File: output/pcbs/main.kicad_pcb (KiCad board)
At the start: 2 copper layers, 142.7 x 177.6 mm, 62 parts

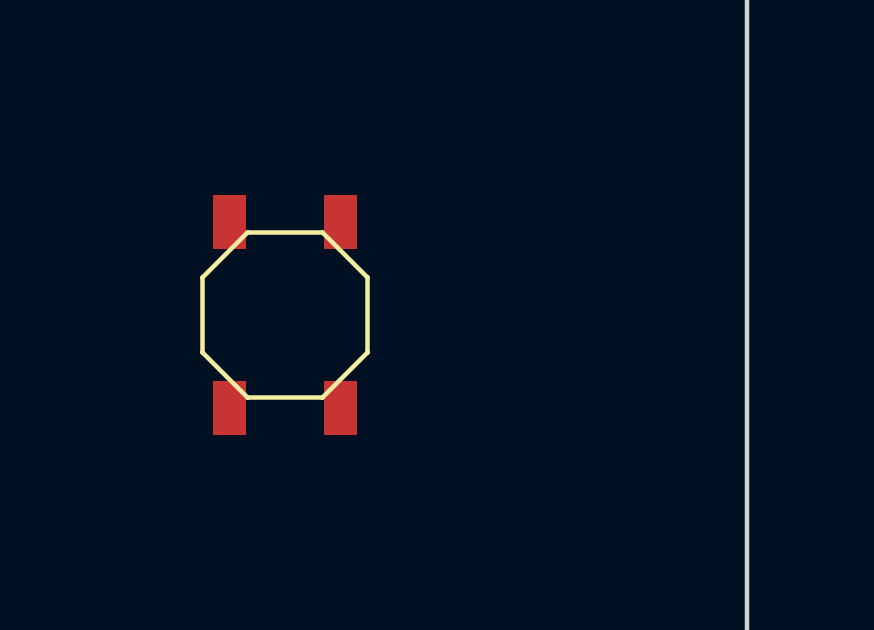
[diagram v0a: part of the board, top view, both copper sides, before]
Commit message: Fix reset position, nets
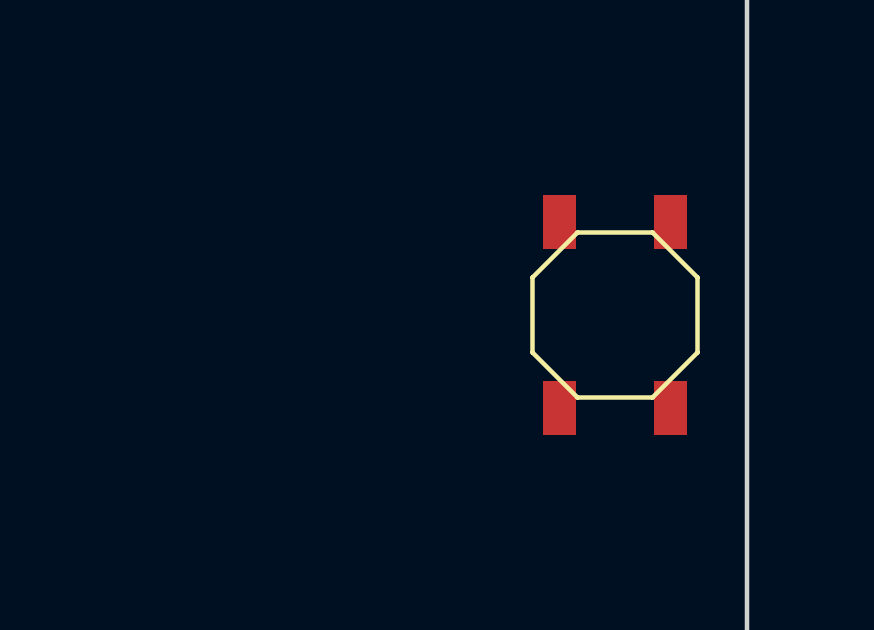
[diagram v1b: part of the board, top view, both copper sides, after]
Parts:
- moved B1 11.0 mm to (225.2, 80.5), turned to -90 degrees
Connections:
- D11 pad 1: P09 -> P9
- D12 pad 1: P08 -> P8
- D15 pad 1: P09 -> P9
- D16 pad 1: P08 -> P8
- D19 pad 1: P09 -> P9
- D20 pad 1: P08 -> P8
- D23 pad 1: P09 -> P9
- D24 pad 1: P08 -> P8
- D3 pad 1: P09 -> P9
- D4 pad 1: P08 -> P8
- D7 pad 1: P09 -> P9
- D8 pad 1: P08 -> P8
- S1 pad 1: P02 -> P2
- S10 pad 1: P04 -> P4
- S11 pad 1: P04 -> P4
- S12 pad 1: P04 -> P4
- S13 pad 1: P05 -> P5
- S14 pad 1: P05 -> P5
- S15 pad 1: P05 -> P5
- S16 pad 1: P05 -> P5
- S17 pad 1: P06 -> P6
- S18 pad 1: P06 -> P6
- S19 pad 1: P06 -> P6
- S2 pad 1: P02 -> P2
- S20 pad 1: P06 -> P6
- S21 pad 1: P07 -> P7
- S22 pad 1: P07 -> P7
- S23 pad 1: P07 -> P7
- S24 pad 1: P07 -> P7
- S25 pad 1: P02 -> P2
- S26 pad 1: P03 -> P3
- S27 pad 1: P04 -> P4
- S28 pad 1: P05 -> P5
- S29 pad 1: P06 -> P6
- S3 pad 1: P02 -> P2
- S30 pad 1: P07 -> P7
- S4 pad 1: P02 -> P2
- S5 pad 1: P03 -> P3
- S6 pad 1: P03 -> P3
- S7 pad 1: P03 -> P3
- S8 pad 1: P03 -> P3
- S9 pad 1: P04 -> P4

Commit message: Nearly viable product
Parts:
- added U?: SW-SMD_3P-P1.50_L2.7-W6.6, Switch:SW-SMD_3P-P1.50_L2.7-W6.6, F.Cu at (227.0, 92.8)
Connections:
- D1 pad 1: P16 -> P5
- D10 pad 1: P10 -> P4
- D11 pad 1: P9 -> P3
- D12 pad 1: P8 -> P2
- D13 pad 1: P16 -> P5
- D14 pad 1: P10 -> P4
- D15 pad 1: P9 -> P3
- D16 pad 1: P8 -> P2
- D17 pad 1: P16 -> P5
- D18 pad 1: P10 -> P4
- D19 pad 1: P9 -> P3
- D2 pad 1: P10 -> P4
- D20 pad 1: P8 -> P2
- D21 pad 1: P16 -> P5
- D22 pad 1: P10 -> P4
- D23 pad 1: P9 -> P3
- D24 pad 1: P8 -> P2
- D3 pad 1: P9 -> P3
- D4 pad 1: P8 -> P2
- D5 pad 1: P16 -> P5
- D6 pad 1: P10 -> P4
- D7 pad 1: P9 -> P3
- D8 pad 1: P8 -> P2
- D9 pad 1: P16 -> P5
- S1 pad 1: P2 -> P6
- S10 pad 1: P4 -> P8
- S11 pad 1: P4 -> P8
- S12 pad 1: P4 -> P8
- S13 pad 1: P5 -> P9
- S14 pad 1: P5 -> P9
- S15 pad 1: P5 -> P9
- S16 pad 1: P5 -> P9
- S17 pad 1: P6 -> P10
- S18 pad 1: P6 -> P10
- S19 pad 1: P6 -> P10
- S2 pad 1: P2 -> P6
- S20 pad 1: P6 -> P10
- S21 pad 1: P7 -> P16
- S22 pad 1: P7 -> P16
- S23 pad 1: P7 -> P16
- S24 pad 1: P7 -> P16
- S25 pad 1: P2 -> P6
- S26 pad 1: P3 -> P7
- S27 pad 1: P4 -> P8
- S28 pad 1: P5 -> P9
- S29 pad 1: P6 -> P10
- S3 pad 1: P2 -> P6
- S30 pad 1: P7 -> P16
- S4 pad 1: P2 -> P6
- S5 pad 1: P3 -> P7
- S6 pad 1: P3 -> P7
- S7 pad 1: P3 -> P7
- S8 pad 1: P3 -> P7
- S9 pad 1: P4 -> P8
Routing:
- net P14: track 0.00 -> 272.6 mm
- net P6: track 0.00 -> 253.7 mm, vias 0 -> 4
- net P7: track 0.00 -> 248.7 mm, vias 0 -> 3
- net P16: track 0.00 -> 244.0 mm, vias 0 -> 2
- net P8: track 0.00 -> 236.5 mm, vias 0 -> 3
- net P10: track 0.00 -> 235.9 mm, vias 0 -> 4
- net P9: track 0.00 -> 235.0 mm, vias 0 -> 4
- net P5: track 0.00 -> 185.3 mm
- net P4: track 0.00 -> 170.1 mm
- net P3: track 0.00 -> 155.5 mm
- net P2: track 0.00 -> 143.7 mm
- net GND: track 0.00 -> 63.5 mm
- net RST: track 0.00 -> 41.1 mm
- net sixth_cluster: track 0.00 -> 15.1 mm
- net second_cluster: track 0.00 -> 15.1 mm
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- added copper zone on B.Cu, net GND
- added copper zone on F.Cu, net GND
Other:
- net class Default removed

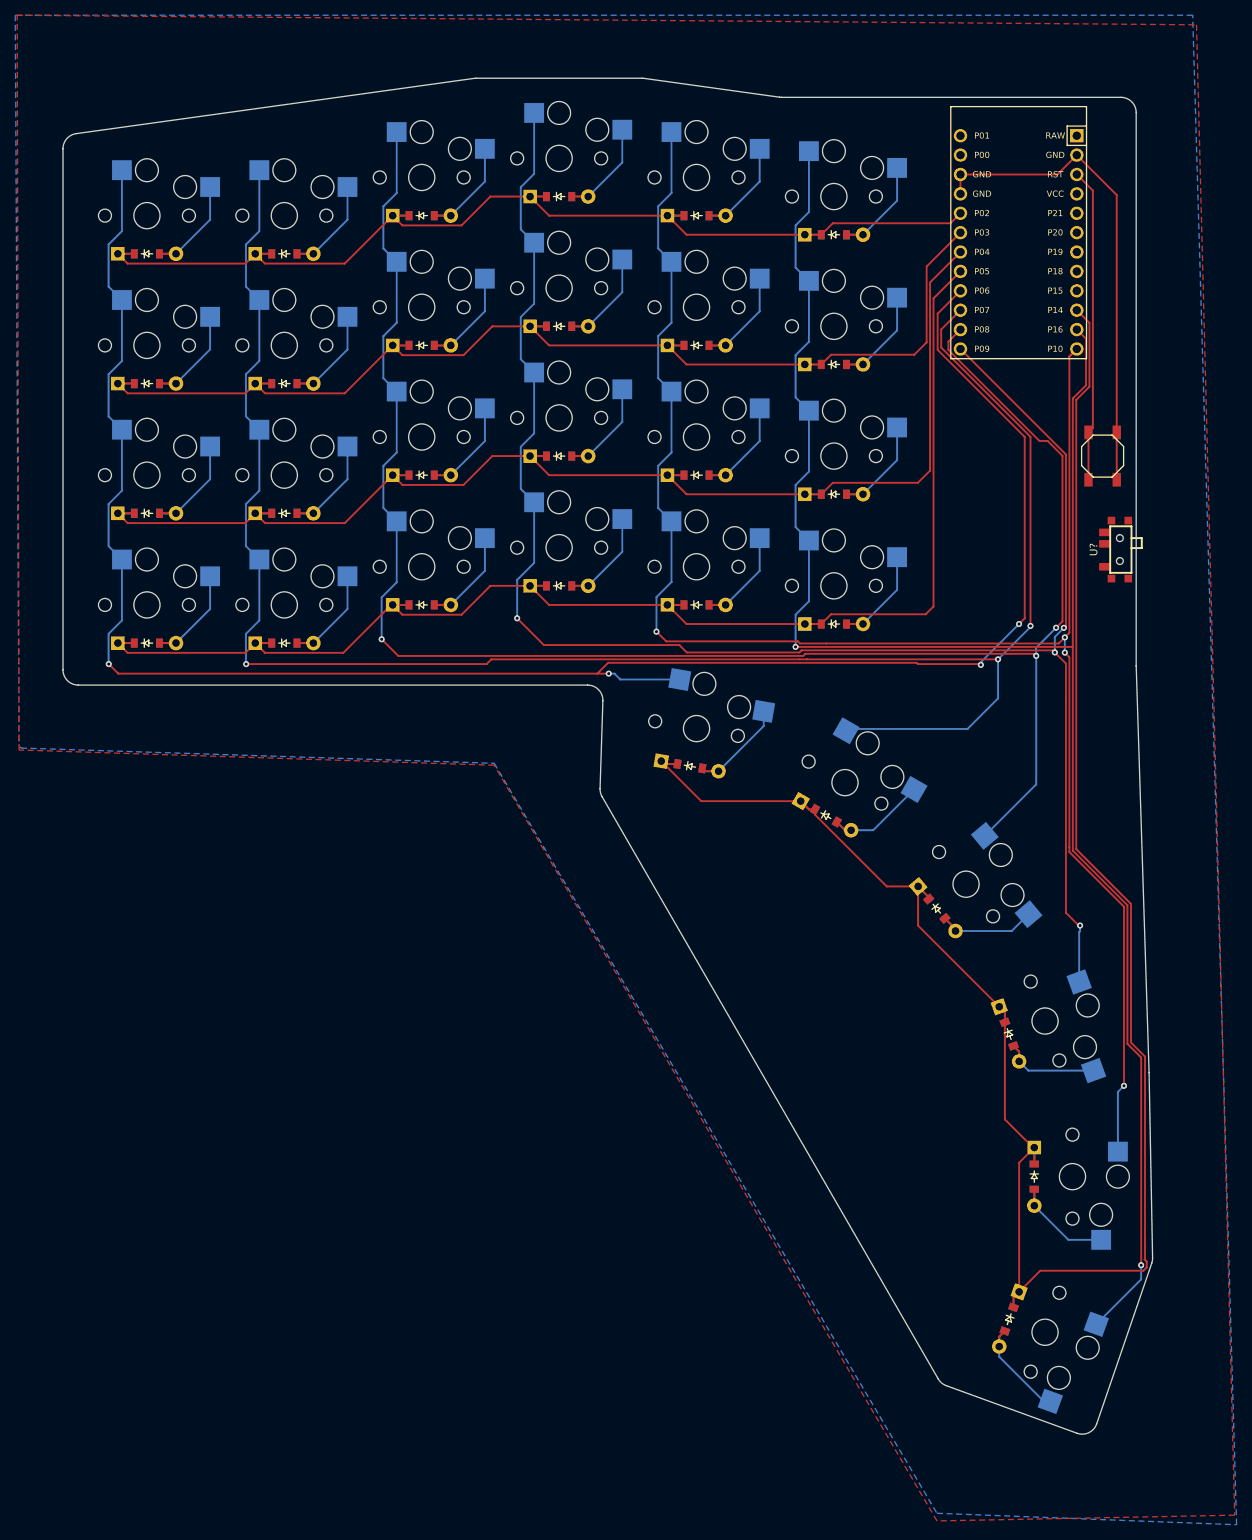
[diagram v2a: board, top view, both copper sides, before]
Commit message: Updating footprints/placement
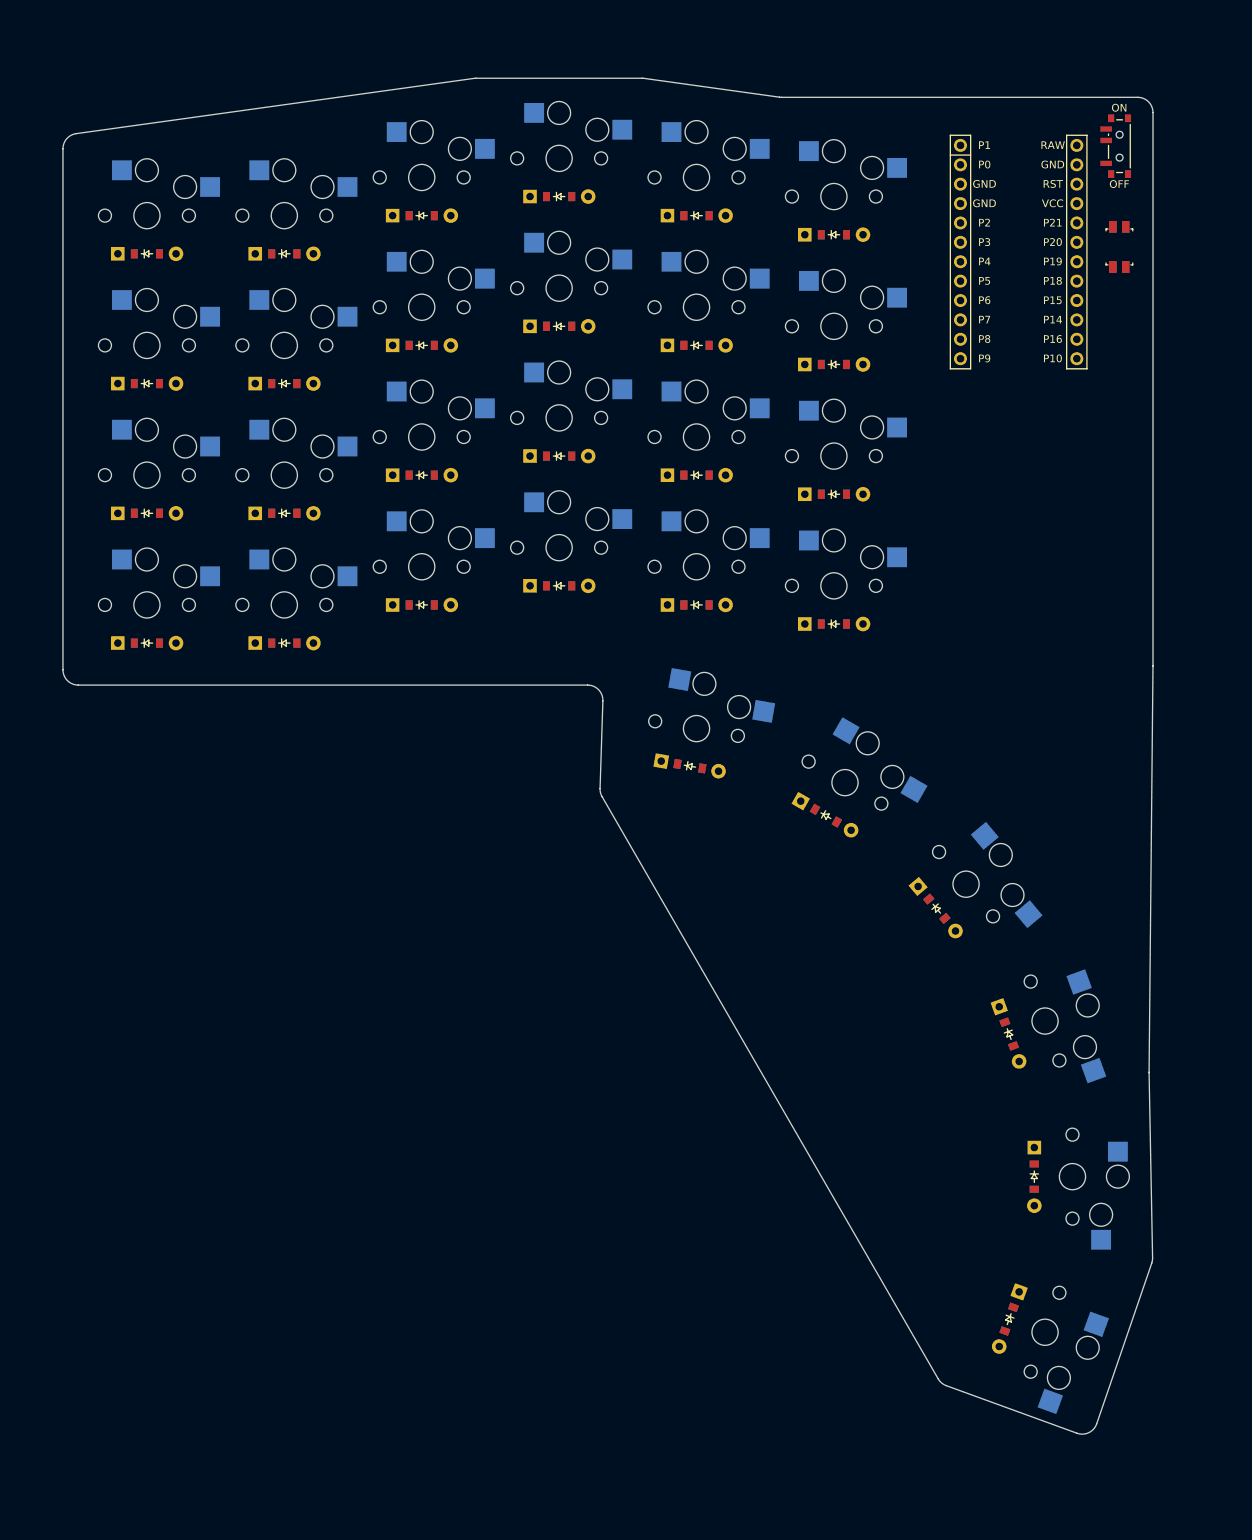
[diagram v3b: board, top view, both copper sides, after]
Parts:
- removed B1: , E73:SW_TACT_ALPS_SKQGABE010
- removed U?: SW-SMD_3P-P1.50_L2.7-W6.6, Switch:SW-SMD_3P-P1.50_L2.7-W6.6
- added PWR1: , ceoloide:power_switch_smd_side, F.Cu at (227.4, 39.9)
- added RST1: , ceoloide:reset_switch_smd_side, F.Cu at (227.4, 53.1)
- MCU1: footprint ProMicro -> ceoloide:mcu_nice_nano
- turned MCU1 to 0 degrees
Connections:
- MCU1 pad 13: P1 -> P9
- MCU1 pad 14: P0 -> P8
- MCU1 pad 15: GND -> P7
- MCU1 pad 16: GND -> P6
- MCU1 pad 17: P2 -> P5
- MCU1 pad 18: P3 -> P4
- MCU1 pad 19: P4 -> P3
- MCU1 pad 20: P5 -> P2
- MCU1 pad 21: P6 -> GND
- MCU1 pad 22: P7 -> GND
- MCU1 pad 23: P8 -> P0
- MCU1 pad 24: P9 -> P1
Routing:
- net P14: track 272.6 -> 0.00 mm
- net P6: track 253.7 -> 0.00 mm, vias 4 -> 0
- net P7: track 248.7 -> 0.00 mm, vias 3 -> 0
- net P16: track 244.0 -> 0.00 mm, vias 2 -> 0
- net P8: track 236.5 -> 0.00 mm, vias 3 -> 0
- net P10: track 235.9 -> 0.00 mm, vias 4 -> 0
- net P9: track 235.0 -> 0.00 mm, vias 4 -> 0
- net P5: track 185.3 -> 0.00 mm
- net P4: track 170.1 -> 0.00 mm
- net P3: track 155.5 -> 0.00 mm
- net P2: track 143.7 -> 0.00 mm
- net GND: track 63.5 -> 0.00 mm
- net RST: track 41.1 -> 0.00 mm
- net sixth_cluster: track 15.1 -> 0.00 mm
- net second_cluster: track 15.1 -> 0.00 mm
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- removed copper zone on B.Cu, net GND
- removed copper zone on F.Cu, net GND
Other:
- board size 142.7 x 177.6 mm -> 142.8 x 177.6 mm

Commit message: Finished left half maybe
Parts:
- moved PWR1 3.45 mm to (230.8, 39.3)
- moved RST1 3.45 mm to (230.8, 53.7)
- moved MCU1 2.42 mm to (216.4, 51.5)
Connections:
- D1 pad 1: P5 -> P16
- D10 pad 1: P4 -> P10
- D11 pad 1: P3 -> P9
- D12 pad 1: P2 -> P8
- D13 pad 1: P5 -> P16
- D14 pad 1: P4 -> P10
- D15 pad 1: P3 -> P9
- D16 pad 1: P2 -> P8
- D17 pad 1: P5 -> P16
- D18 pad 1: P4 -> P10
- D19 pad 1: P3 -> P9
- D2 pad 1: P4 -> P10
- D20 pad 1: P2 -> P8
- D21 pad 1: P5 -> P16
- D22 pad 1: P4 -> P10
- D23 pad 1: P3 -> P9
- D24 pad 1: P2 -> P8
- D3 pad 1: P3 -> P9
- D4 pad 1: P2 -> P8
- D5 pad 1: P5 -> P16
- D6 pad 1: P4 -> P10
- D7 pad 1: P3 -> P9
- D8 pad 1: P2 -> P8
- D9 pad 1: P5 -> P16
- S1 pad 1: P6 -> P2
- S10 pad 1: P8 -> P4
- S11 pad 1: P8 -> P4
- S12 pad 1: P8 -> P4
- S13 pad 1: P9 -> P5
- S14 pad 1: P9 -> P5
- S15 pad 1: P9 -> P5
- S16 pad 1: P9 -> P5
- S17 pad 1: P10 -> P6
- S18 pad 1: P10 -> P6
- S19 pad 1: P10 -> P6
- S2 pad 1: P6 -> P2
- S20 pad 1: P10 -> P6
- S21 pad 1: P16 -> P7
- S22 pad 1: P16 -> P7
- S23 pad 1: P16 -> P7
- S24 pad 1: P16 -> P7
- S25 pad 1: P6 -> P2
- S26 pad 1: P7 -> P3
- S27 pad 1: P8 -> P4
- S28 pad 1: P9 -> P5
- S29 pad 1: P10 -> P6
- S3 pad 1: P6 -> P2
- S30 pad 1: P16 -> P7
- S4 pad 1: P6 -> P2
- S5 pad 1: P7 -> P3
- S6 pad 1: P7 -> P3
- S7 pad 1: P7 -> P3
- S8 pad 1: P7 -> P3
- S9 pad 1: P8 -> P4
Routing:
- net P2: track 0.00 -> 295.6 mm, vias 0 -> 3
- net P3: track 0.00 -> 286.6 mm, vias 0 -> 3
- net P4: track 0.00 -> 266.8 mm, vias 0 -> 3
- net P5: track 0.00 -> 255.2 mm, vias 0 -> 3
- net P6: track 0.00 -> 253.6 mm, vias 0 -> 3
- net P7: track 0.00 -> 242.2 mm, vias 0 -> 3
- net P14: track 0.00 -> 208.8 mm, vias 0 -> 2
- net P16: track 0.00 -> 182.9 mm
- net P10: track 0.00 -> 160.4 mm
- net P8: track 0.00 -> 142.5 mm
- net P9: track 0.00 -> 139.3 mm
- net GND: track 0.00 -> 37.0 mm
- net sixth_cluster: track 0.00 -> 16.5 mm
- net fourth_cluster: track 0.00 -> 16.4 mm
- net second_cluster: track 0.00 -> 16.2 mm
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- added copper zone on B.Cu, net GND
- added copper zone on F.Cu, net GND
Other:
- board size 142.8 x 177.6 mm -> 147.6 x 179.9 mm

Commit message: Start adding mirrored right layer with alternate nets
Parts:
- added D31: , ComboDiode, F.Cu at (520.0, 105.0)
- added D32: , ComboDiode, F.Cu at (520.0, 88.0)
- added D33: , ComboDiode, F.Cu at (520.0, 71.0)
- added D34: , ComboDiode, F.Cu at (520.0, 54.0)
- added D35: , ComboDiode, F.Cu at (502.0, 105.0)
- added D36: , ComboDiode, F.Cu at (502.0, 88.0)
- added D37: , ComboDiode, F.Cu at (502.0, 71.0)
- added D38: , ComboDiode, F.Cu at (502.0, 54.0)
- added D39: , ComboDiode, F.Cu at (484.0, 100.0)
- added D40: , ComboDiode, F.Cu at (484.0, 83.0)
- added D41: , ComboDiode, F.Cu at (484.0, 66.0)
- added D42: , ComboDiode, F.Cu at (484.0, 49.0)
- added D43: , ComboDiode, F.Cu at (466.0, 97.5)
- added D44: , ComboDiode, F.Cu at (466.0, 80.5)
- added D45: , ComboDiode, F.Cu at (466.0, 63.5)
- added D46: , ComboDiode, F.Cu at (466.0, 46.5)
- added D47: , ComboDiode, F.Cu at (448.0, 100.0)
- added D48: , ComboDiode, F.Cu at (448.0, 83.0)
- added D49: , ComboDiode, F.Cu at (448.0, 66.0)
- added D50: , ComboDiode, F.Cu at (448.0, 49.0)
- added D51: , ComboDiode, F.Cu at (430.0, 102.5)
- added D52: , ComboDiode, F.Cu at (430.0, 85.5)
- added D53: , ComboDiode, F.Cu at (430.0, 68.5)
- added D54: , ComboDiode, F.Cu at (430.0, 51.5)
- added D55: , ComboDiode, F.Cu at (448.9, 121.1)
- added D56: , ComboDiode, F.Cu at (430.2, 127.9)
- added D57: , ComboDiode, F.Cu at (415.0, 140.7)
- added D58: , ComboDiode, F.Cu at (405.1, 157.9)
- added D59: , ComboDiode, F.Cu at (401.6, 177.4)
- added D60: , ComboDiode, F.Cu at (405.1, 197.0)
- added MCU2: , ceoloide:mcu_nice_nano, F.Cu at (403.6, 52.0)
- added PWR2: , ceoloide:power_switch_smd_side, F.Cu at (389.2, 39.6)
- added RST2: , ceoloide:reset_switch_smd_side, F.Cu at (389.2, 53.4)
- added S31: , PG1350, F.Cu at (520.0, 100.0)
- added S32: , PG1350, F.Cu at (520.0, 83.0)
- added S33: , PG1350, F.Cu at (520.0, 66.0)
- added S34: , PG1350, F.Cu at (520.0, 49.0)
- added S35: , PG1350, F.Cu at (502.0, 100.0)
- added S36: , PG1350, F.Cu at (502.0, 83.0)
- added S37: , PG1350, F.Cu at (502.0, 66.0)
- added S38: , PG1350, F.Cu at (502.0, 49.0)
- added S39: , PG1350, F.Cu at (484.0, 95.0)
- added S40: , PG1350, F.Cu at (484.0, 78.0)
- added S41: , PG1350, F.Cu at (484.0, 61.0)
- added S42: , PG1350, F.Cu at (484.0, 44.0)
- added S43: , PG1350, F.Cu at (466.0, 92.5)
- added S44: , PG1350, F.Cu at (466.0, 75.5)
- added S45: , PG1350, F.Cu at (466.0, 58.5)
- added S46: , PG1350, F.Cu at (466.0, 41.5)
- added S47: , PG1350, F.Cu at (448.0, 95.0)
- added S48: , PG1350, F.Cu at (448.0, 78.0)
- added S49: , PG1350, F.Cu at (448.0, 61.0)
- added S50: , PG1350, F.Cu at (448.0, 44.0)
- added S51: , PG1350, F.Cu at (430.0, 97.5)
- added S52: , PG1350, F.Cu at (430.0, 80.5)
- added S53: , PG1350, F.Cu at (430.0, 63.5)
- added S54: , PG1350, F.Cu at (430.0, 46.5)
- added S55: , PG1350, F.Cu at (448.0, 116.2)
- added S56: , PG1350, F.Cu at (427.7, 123.6)
- added S57: , PG1350, F.Cu at (411.2, 137.5)
- added S58: , PG1350, F.Cu at (400.4, 156.2)
- added S59: , PG1350, F.Cu at (396.6, 177.4)
- added S60: , PG1350, F.Cu at (400.4, 198.7)
- moved S30 3.97 mm to (219.6, 198.7)
- moved D30 3.97 mm to (214.9, 197.0)
- moved D29 3.33 mm to (218.4, 177.4)
- moved S29 3.33 mm to (223.4, 177.4)
- moved S28 2.59 mm to (219.6, 156.2)
- moved D28 2.59 mm to (214.9, 157.9)
- moved S27 1.77 mm to (208.8, 137.5)
- moved D27 1.77 mm to (205.0, 140.7)
- moved D26 0.90 mm to (189.8, 127.9)
- moved S26 0.90 mm to (192.3, 123.6)
- moved MCU1 0.50 mm to (216.4, 52.0)
- moved PWR1 0.30 mm to (230.8, 39.6)
- moved RST1 0.30 mm to (230.8, 53.4)
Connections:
- S5 pad 1: P3 -> P23
- S6 pad 1: P3 -> P23
- S7 pad 1: P3 -> P23
- S8 pad 1: P3 -> P23
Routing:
- net P2: track 295.6 -> 0.00 mm, vias 3 -> 0
- net P3: track 286.6 -> 0.00 mm, vias 3 -> 0
- net P4: track 266.8 -> 0.00 mm, vias 3 -> 0
- net P5: track 255.2 -> 0.00 mm, vias 3 -> 0
- net P6: track 253.6 -> 0.00 mm, vias 3 -> 0
- net P7: track 242.2 -> 0.00 mm, vias 3 -> 0
- net P14: track 208.8 -> 0.00 mm, vias 2 -> 0
- net P16: track 182.9 -> 0.00 mm
- net P10: track 160.4 -> 0.00 mm
- net P8: track 142.5 -> 0.00 mm
- net P9: track 139.3 -> 0.00 mm
- net GND: track 37.0 -> 0.00 mm
- net sixth_cluster: track 16.5 -> 0.00 mm
- net fourth_cluster: track 16.4 -> 0.00 mm
- net second_cluster: track 16.2 -> 0.00 mm
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- removed copper zone on B.Cu, net GND
- removed copper zone on F.Cu, net GND
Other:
- board size 147.6 x 179.9 mm -> 444 x 183.4 mm
- net class Default added: clearance 0.2, trace_width 0.25, via_dia 0.8, via_drill 0.4

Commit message: Adding mounting holes
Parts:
- added H1: , ceoloide:mounting_hole_plated, F.Cu at (109.0, 57.5)
- added H10: , ceoloide:mounting_hole_plated, F.Cu at (418.0, 166.5)
- added H2: , ceoloide:mounting_hole_plated, F.Cu at (511.0, 57.5)
- added H3: , ceoloide:mounting_hole_plated, F.Cu at (109.0, 91.5)
- added H4: , ceoloide:mounting_hole_plated, F.Cu at (511.0, 91.5)
- added H5: , ceoloide:mounting_hole_plated, F.Cu at (230.8, 37.3)
- added H6: , ceoloide:mounting_hole_plated, F.Cu at (389.2, 37.3)
- added H7: , ceoloide:mounting_hole_plated, F.Cu at (214.0, 97.5)
- added H8: , ceoloide:mounting_hole_plated, F.Cu at (406.0, 97.5)
- added H9: , ceoloide:mounting_hole_plated, F.Cu at (202.0, 166.5)
- moved PWR1 6.90 mm to (230.8, 46.5)
- moved PWR2 6.90 mm to (389.2, 46.5)
- moved RST1 6.90 mm to (230.8, 60.3)
- moved RST2 6.90 mm to (389.2, 60.3)
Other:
- net class Default removed

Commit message: Add attribution
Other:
- net class Default added: clearance 0.2, trace_width 0.25, via_dia 0.8, via_drill 0.4
- board text added: "By Dylan Bulfin"
- board text added: "using Ergogen"
